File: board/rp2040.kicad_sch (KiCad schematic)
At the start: 19 parts, among them U1 W25Q16JVUXIQ, U2 RP2040, Y1 12MhZ

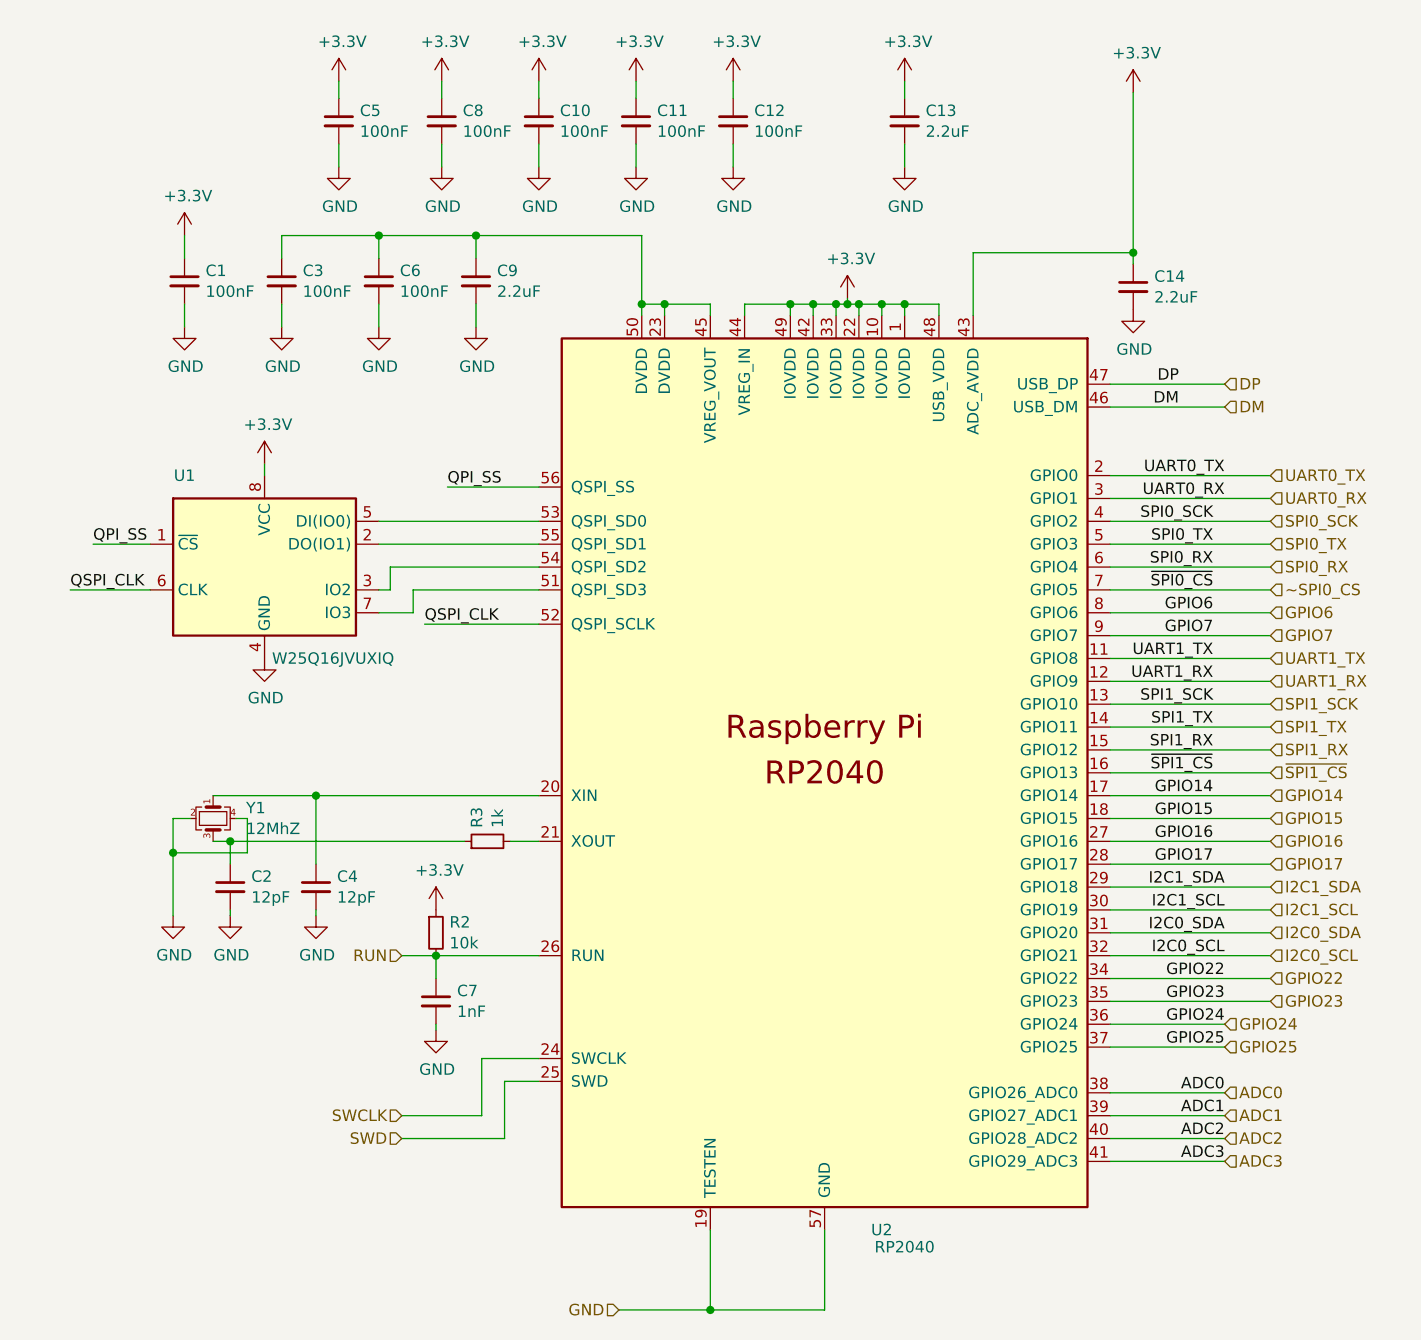
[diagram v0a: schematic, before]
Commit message: added boot select button
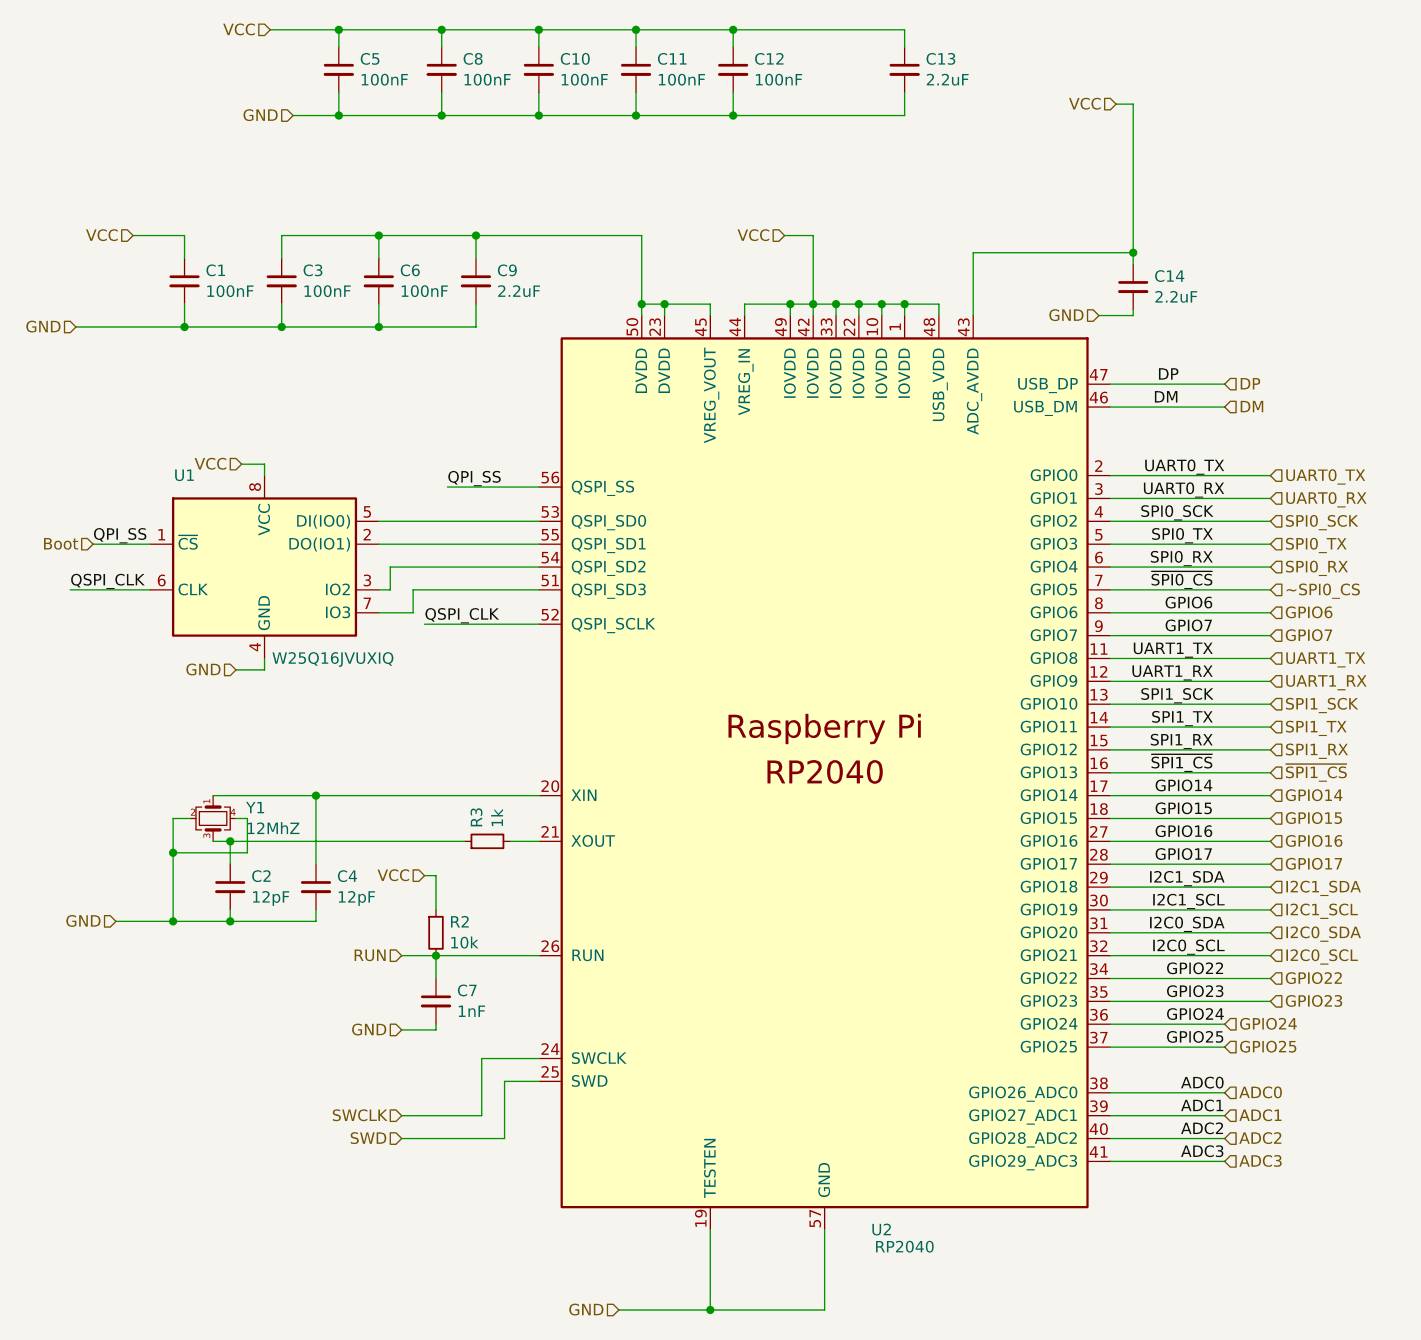
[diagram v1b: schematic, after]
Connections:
- net +3V3 renamed VCC
- net QPI_SS renamed Boot
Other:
- moved on the sheet: C10, C11, C12, C13, C5, C8

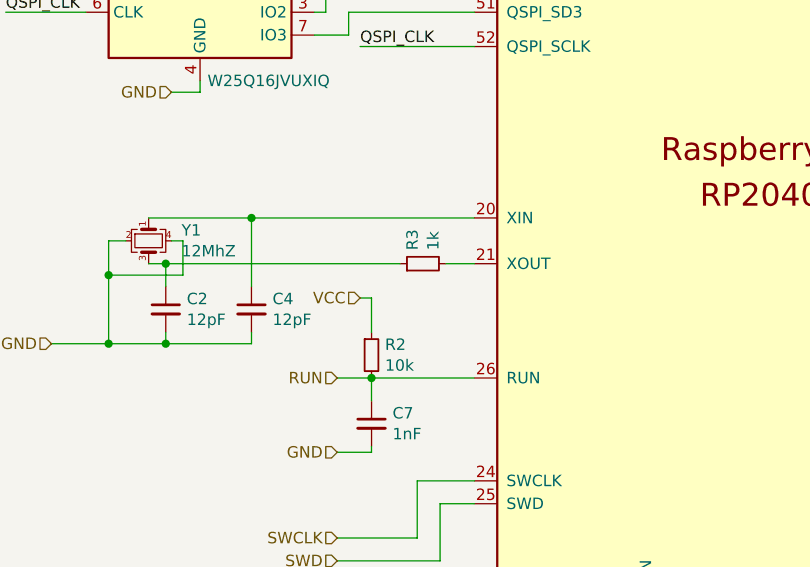
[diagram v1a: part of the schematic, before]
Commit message: added straping support for different interfaces
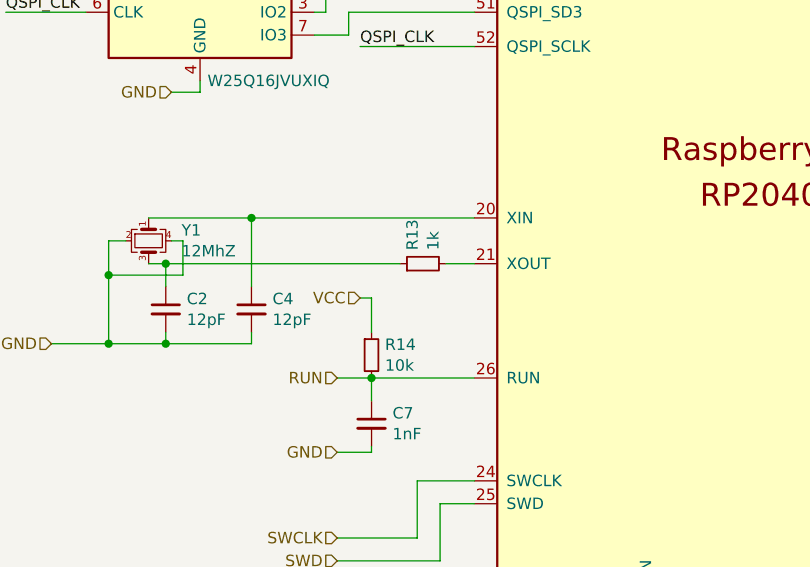
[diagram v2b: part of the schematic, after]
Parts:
- renumbered R3 to R13, R2 to R14
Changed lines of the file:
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@@
   (symbol (lib_id "Device:R_Small") (at 90.17 127 0) (unit 1)
     (in_bom yes) (on_board yes) (dnp no)
-    (property "Reference" "R2" (at 91.6686 125.8316 0)
+    (property "Reference" "R14" (at 91.6686 125.8316 0)
       (effects (font (size 1.27 1.27)) (justify left))
     )
@@
       (project "board"
         (path "/57732dd3-1162-4c3f-88bd-31bf473d124d/d7f4faf0-6611-4124-99f4-3c5e31784302"
-          (reference "R2") (unit 1)
+          (reference "R14") (unit 1)
         )
       )
@@
   (symbol (lib_id "Device:R_Small") (at 95.885 116.84 90) (unit 1)
     (in_bom yes) (on_board yes) (dnp no)
-    (property "Reference" "R3" (at 94.7166 115.3414 0)
+    (property "Reference" "R13" (at 94.7166 115.3414 0)
       (effects (font (size 1.27 1.27)) (justify left))
     )
@@
       (project "board"
         (path "/57732dd3-1162-4c3f-88bd-31bf473d124d/d7f4faf0-6611-4124-99f4-3c5e31784302"
-          (reference "R3") (unit 1)
+          (reference "R13") (unit 1)
         )
       )
